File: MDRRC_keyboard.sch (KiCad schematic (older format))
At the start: 16 parts

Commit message: Fixed two small errors
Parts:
- gave numbers to parts that had none: 16
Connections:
- net GND: now also CON1.6
- net VCC: now also C4.1, P3.1 (P1), R4.1, R5.1
- net at IC1.8 (PB7(XTAL2/TOSC2)), P2.8 (P8): no longer CON1.6
- new net: D1.2 (K), IC1.14 ((~SS~/OC1B)PB2)
- no-connect marks 0 -> 12
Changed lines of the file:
@@
-EESchema Schematic File Version 2  date Sunday, 2013 September 29 10:10:44
+EESchema Schematic File Version 2  date Sunday, 2013 September 29 16:19:32
 LIBS:power
 LIBS:device
@@
 LIBS:valves
 LIBS:pyth
+LIBS:MDRRC_keyboard-cache
 EELAYER 27 0
 EELAYER END
@@
 $EndDescr
 $Comp
-L LCD P?
+L LCD P1
 U 1 1 52473158
 P 6750 3100
-F 0 "P?" V 6850 3100 60  0000 C CNN
+F 0 "P1" V 6850 3100 60  0000 C CNN
 F 1 "LCD" V 6950 3100 60  0000 C CNN
 F 2 "" H 6750 3100 60  0000 C CNN
@@
 	10650 2850 10750 2950
 $Comp
-L ATMEGA8-AI IC?
+L ATMEGA8-AI IC1
 U 1 1 52473167
 P 4350 3200
-F 0 "IC?" H 3650 4350 50  0000 L BNN
+F 0 "IC1" H 3650 4350 50  0000 L BNN
 F 1 "ATMEGA8-AI" H 4650 1700 50  0000 L BNN
 F 2 "TQFP32" H 3800 1750 50  0001 C CNN
@@
 $EndComp
 $Comp
-L CONN_8 P?
+L CONN_8 P2
 U 1 1 52473176
 P 6750 4350
-F 0 "P?" V 6700 4350 60  0000 C CNN
+F 0 "P2" V 6700 4350 60  0000 C CNN
 F 1 "CONN_8" V 6800 4350 60  0000 C CNN
 F 2 "" H 6750 4350 60  0000 C CNN
@@
 Wire Wire Line
 	6050 4600 6400 4600
-Wire Wire Line
-	3450 3100 3400 3100
-Wire Wire Line
-	3400 3100 3400 4700
-Wire Wire Line
-	3200 4700 6400 4700
-$Comp
-L GND #PWR?
+$Comp
+L GND #PWR01
 U 1 1 524731E3
 P 4350 4900
-F 0 "#PWR?" H 4350 4900 30  0001 C CNN
+F 0 "#PWR01" H 4350 4900 30  0001 C CNN
 F 1 "GND" H 4350 4830 30  0001 C CNN
 F 2 "" H 4350 4900 60  0000 C CNN
@@
 $EndComp
 $Comp
-L GND #PWR?
+L GND #PWR02
 U 1 1 524731F2
 P 6250 4900
-F 0 "#PWR?" H 6250 4900 30  0001 C CNN
+F 0 "#PWR02" H 6250 4900 30  0001 C CNN
 F 1 "GND" H 6250 4830 30  0001 C CNN
 F 2 "" H 6250 4900 60  0000 C CNN
@@
 	4300 4800 4300 4850
 Wire Wire Line
-	4300 4850 4400 4850
+	3200 4850 4400 4850
 Wire Wire Line
 	4350 4850 4350 4900
@@
 Connection ~ 4350 4850
 $Comp
-L VCC #PWR?
+L VCC #PWR03
 U 1 1 52473237
 P 4350 1800
-F 0 "#PWR?" H 4350 1900 30  0001 C CNN
+F 0 "#PWR03" H 4350 1900 30  0001 C CNN
 F 1 "VCC" H 4350 1900 30  0000 C CNN
 F 2 "" H 4350 1800 60  0000 C CNN
@@
 $EndComp
 $Comp
-L VCC #PWR?
+L VCC #PWR04
 U 1 1 52473246
 P 6350 1800
-F 0 "#PWR?" H 6350 1900 30  0001 C CNN
+F 0 "#PWR04" H 6350 1900 30  0001 C CNN
 F 1 "VCC" H 6350 1900 30  0000 C CNN
 F 2 "" H 6350 1800 60  0000 C CNN
@@
 Connection ~ 4350 1850
 $Comp
-L POT RV?
+L POT RV1
 U 1 1 524732F4
 P 6050 1900
-F 0 "RV?" H 6050 1800 50  0000 C CNN
+F 0 "RV1" H 6050 1800 50  0000 C CNN
 F 1 "10k" H 6050 1900 50  0000 C CNN
 F 2 "" H 6050 1900 60  0000 C CNN
@@
 $EndComp
 Wire Wire Line
-	6300 1900 6350 1900
+	6300 1900 7500 1900
 Connection ~ 6350 1900
 Wire Wire Line
@@
 	5800 3600 6400 3600
 $Comp
-L C C?
+L C C3
 U 1 1 5247DC1C
 P 3150 2850
-F 0 "C?" H 3200 2950 50  0000 L CNN
+F 0 "C3" H 3200 2950 50  0000 L CNN
 F 1 "100nF" H 3200 2750 50  0000 L CNN
 F 2 "" H 3150 2850 60  0000 C CNN
@@
 Wire Wire Line
 	3150 2350 3150 2650
-Wire Wire Line
-	2700 2400 3450 2400
 Connection ~ 3150 2500
 $Comp
-L VCC #PWR?
+L VCC #PWR05
 U 1 1 5247DCDF
 P 3150 2350
-F 0 "#PWR?" H 3150 2450 30  0001 C CNN
+F 0 "#PWR05" H 3150 2450 30  0001 C CNN
 F 1 "VCC" H 3150 2450 30  0000 C CNN
 F 2 "" H 3150 2350 60  0000 C CNN
@@
 $EndComp
 $Comp
-L GND #PWR?
+L GND #PWR06
 U 1 1 5247DCEE
 P 3050 3150
-F 0 "#PWR?" H 3050 3150 30  0001 C CNN
+F 0 "#PWR06" H 3050 3150 30  0001 C CNN
 F 1 "GND" H 3050 3080 30  0001 C CNN
 F 2 "" H 3050 3150 60  0000 C CNN
@@
 Connection ~ 3150 2400
 $Comp
-L C C?
+L C C2
 U 1 1 5247DE1A
 P 2700 2850
-F 0 "C?" H 2750 2950 50  0000 L CNN
+F 0 "C2" H 2750 2950 50  0000 L CNN
 F 1 "100nF" H 2750 2750 50  0000 L CNN
 F 2 "" H 2700 2850 60  0000 C CNN
@@
 $EndComp
 Wire Wire Line
-	2700 2650 2700 2400
-Wire Wire Line
 	2700 3050 2700 3100
 Connection ~ 2950 3100
 $Comp
-L C C?
+L C C1
 U 1 1 5247DEB3
 P 2400 2850
-F 0 "C?" H 2450 2950 50  0000 L CNN
+F 0 "C1" H 2450 2950 50  0000 L CNN
 F 1 "100nF" H 2450 2750 50  0000 L CNN
 F 2 "" H 2400 2850 60  0000 C CNN
@@
 $EndComp
 $Comp
-L R R?
+L R R1
 U 1 1 5247DEC2
 P 3350 1850
-F 0 "R?" V 3430 1850 50  0000 C CNN
+F 0 "R1" V 3430 1850 50  0000 C CNN
 F 1 "10k" V 3350 1850 50  0000 C CNN
 F 2 "" H 3350 1850 60  0000 C CNN
@@
 Connection ~ 3050 1850
 $Comp
-L R R?
+L R R3
 U 1 1 5247E01F
 P 7250 3500
-F 0 "R?" V 7330 3500 50  0000 C CNN
+F 0 "R3" V 7330 3500 50  0000 C CNN
 F 1 "1k" V 7250 3500 50  0000 C CNN
 F 2 "" H 7250 3500 60  0000 C CNN
@@
 $EndComp
 $Comp
-L LED D?
+L LED D1
 U 1 1 5247E02E
 P 7250 2950
-F 0 "D?" H 7250 3050 50  0000 C CNN
+F 0 "D1" H 7250 3050 50  0000 C CNN
 F 1 "LED" H 7250 2850 50  0000 C CNN
 F 2 "" H 7250 2950 60  0000 C CNN
@@
 	6000 2400 6000 2150
 Wire Wire Line
-	6000 2150 7850 2150
-Wire Wire Line
 	7250 2150 7250 2750
 Wire Wire Line
@@
 Connection ~ 6250 4800
 $Comp
-L CONN_4 P?
+L CONN_4 P3
 U 1 1 5247E156
 P 8250 3300
-F 0 "P?" V 8200 3300 50  0000 C CNN
+F 0 "P3" V 8200 3300 50  0000 C CNN
 F 1 "CONN_4" V 8300 3300 50  0000 C CNN
 F 2 "" H 8250 3300 60  0000 C CNN
@@
 Wire Wire Line
 	7850 2150 7850 3150
-Connection ~ 7250 2150
 Text Label 5500 3300 0    60   ~ 0
 SDA
@@
 	7500 3350 7900 3350
 $Comp
-L R R?
+L R R4
 U 1 1 5247E4A3
 P 7500 2700
-F 0 "R?" V 7580 2700 50  0000 C CNN
+F 0 "R4" V 7580 2700 50  0000 C CNN
 F 1 "10k" V 7500 2700 50  0000 C CNN
 F 2 "" H 7500 2700 60  0000 C CNN
@@
 $EndComp
 $Comp
-L R R?
+L R R5
 U 1 1 5247E4B2
 P 7700 2700
-F 0 "R?" V 7780 2700 50  0000 C CNN
+F 0 "R5" V 7780 2700 50  0000 C CNN
 F 1 "10k" V 7700 2700 50  0000 C CNN
 F 2 "" H 7700 2700 60  0000 C CNN
@@
 Connection ~ 7700 2150
 Wire Wire Line
-	7500 2450 7500 2150
+	7500 1900 7500 2450
 Connection ~ 7500 2150
 $Comp
-L C C?
+L C C4
 U 1 1 5247E729
 P 7800 3950
-F 0 "C?" H 7850 4050 50  0000 L CNN
+F 0 "C4" H 7850 4050 50  0000 L CNN
 F 1 "100nF" H 7850 3850 50  0000 L CNN
 F 2 "" H 7800 3950 60  0000 C CNN
@@
 Connection ~ 6250 3800
 $Comp
-L R R?
+L R R2
 U 1 1 5247E934
 P 5800 3700
-F 0 "R?" V 5880 3700 50  0000 C CNN
+F 0 "R2" V 5880 3700 50  0000 C CNN
 F 1 "4k7" V 5800 3700 50  0000 C CNN
 F 2 "" H 5800 3700 60  0000 C CNN
@@
 Connection ~ 4400 1850
 Wire Wire Line
-	3200 4250 3200 4700
-Connection ~ 3400 4700
-Wire Wire Line
-	3300 4050 3300 2400
+	3200 4250 3200 4850
+Wire Wire Line
+	3300 2400 3300 4050
 Connection ~ 3300 2400
 Wire Wire Line
@@
 Connection ~ 3050 2200
 $Comp
-L AVR-ISP-6 CON?
+L AVR-ISP-6 CON1
 U 1 1 5247F672
 P 2800 4150
-F 0 "CON?" H 2720 4390 50  0000 C CNN
+F 0 "CON1" H 2720 4390 50  0000 C CNN
 F 1 "AVR-ISP-6" H 2560 3920 50  0000 L BNN
 F 2 "AVR-ISP-6" V 2280 4190 50  0001 C CNN
@@
 $EndComp
 Wire Wire Line
-	2950 4050 3300 4050
+	3300 4050 2950 4050
 Wire Wire Line
 	2950 4250 3200 4250
@@
 	5700 2100 5700 2700
 Connection ~ 5700 2700
+NoConn ~ 5300 2250
+NoConn ~ 5350 2300
+NoConn ~ 5350 2900
+NoConn ~ 5350 3500
+NoConn ~ 5350 3600
+NoConn ~ 5350 3800
+NoConn ~ 5350 3900
+NoConn ~ 3450 2900
+NoConn ~ 6400 2900
+NoConn ~ 6400 3000
+NoConn ~ 6400 3200
+NoConn ~ 6400 3100
+Wire Wire Line
+	2700 2650 2700 2400
+Wire Wire Line
+	2700 2400 3450 2400
+Wire Wire Line
+	6000 2150 7250 2150
+Wire Wire Line
+	7500 2150 7850 2150
+Wire Wire Line
+	3450 3100 3400 3100
+Wire Wire Line
+	3400 3100 3400 4750
+Wire Wire Line
+	3400 4750 6200 4750
+Wire Wire Line
+	6200 4750 6200 4700
+Wire Wire Line
+	6200 4700 6400 4700
+Connection ~ 4300 4850
 $EndSCHEMATC

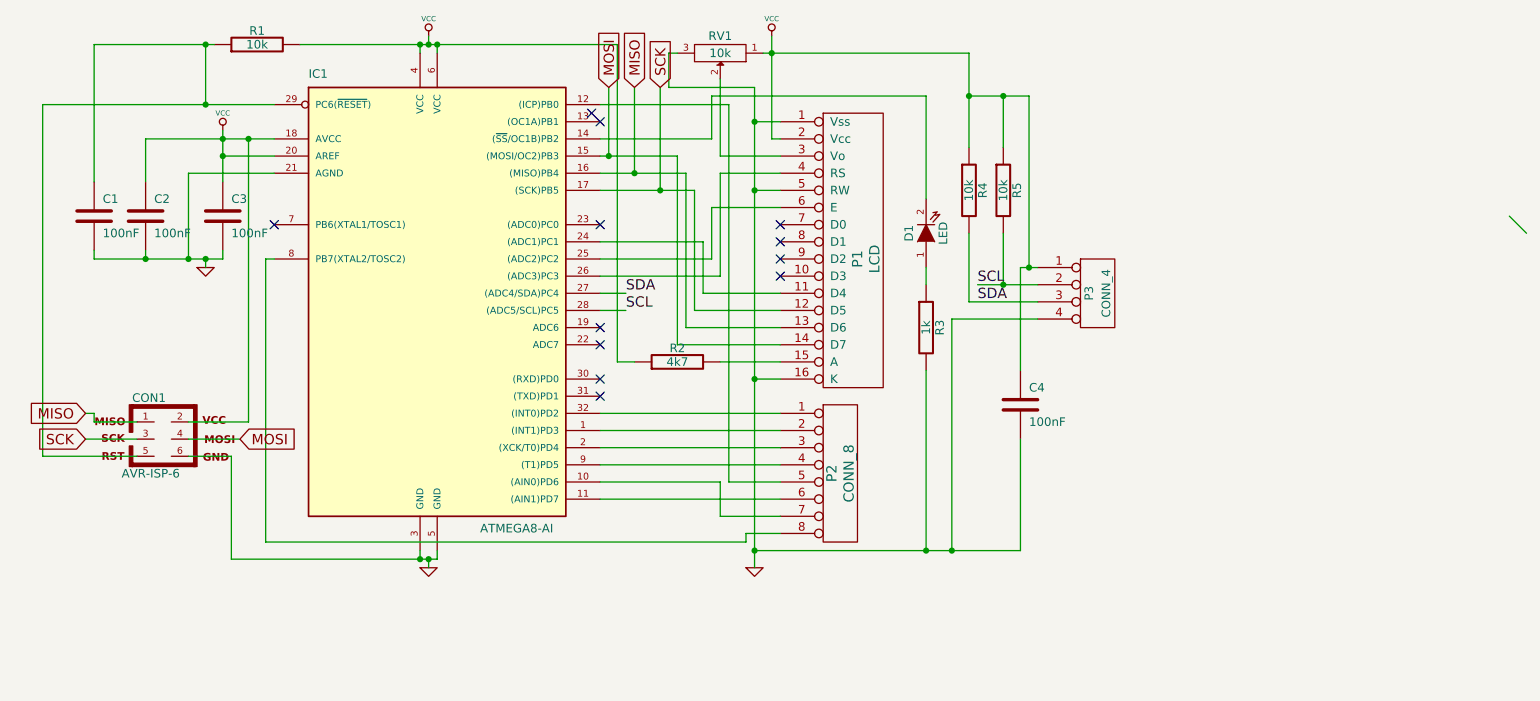
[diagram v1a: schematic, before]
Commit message: Added possibility for crystal and broke out remaining I/O to header
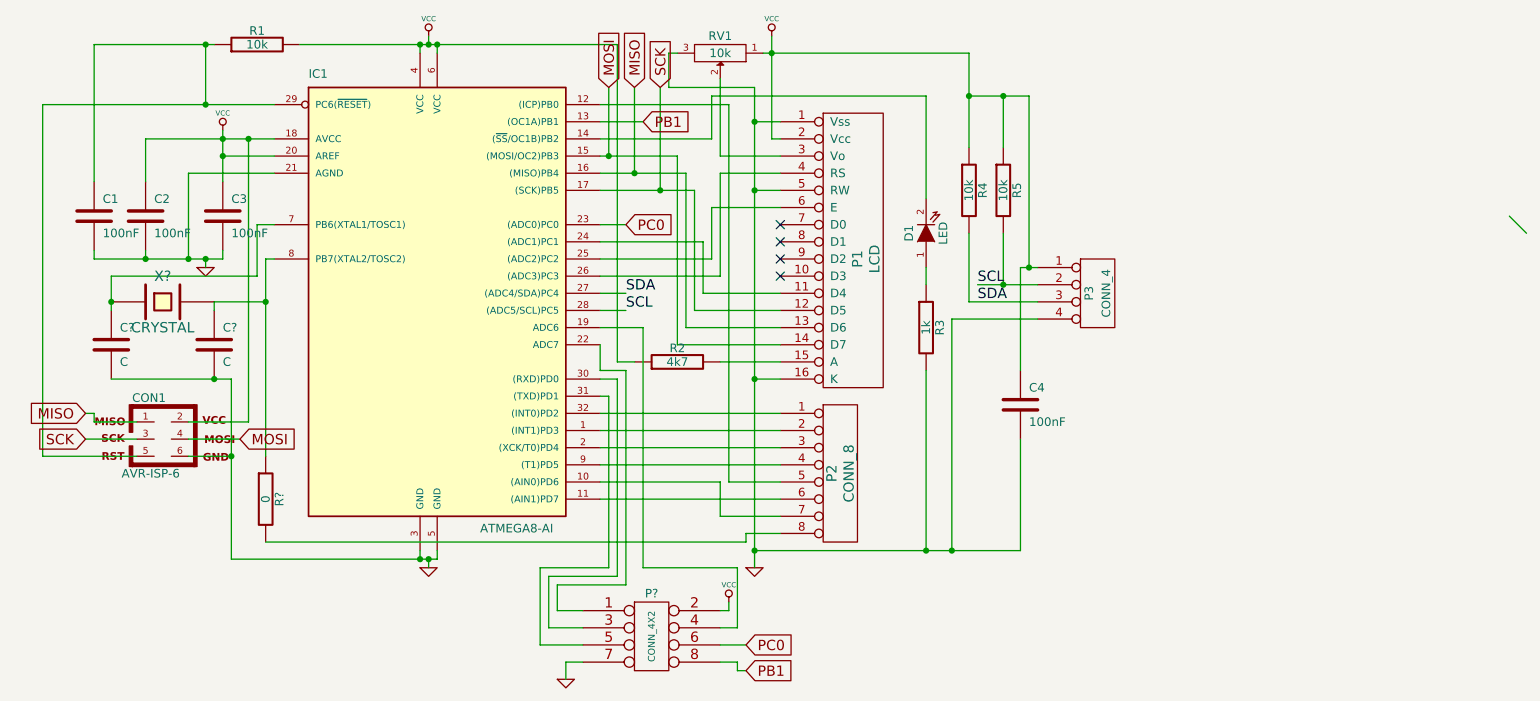
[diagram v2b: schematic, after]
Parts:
- added C? (x2): C, symbol C
- added P?: CONN_4X2, symbol CONN_4X2
- added R?: 0, symbol R
- added X?: CRYSTAL, symbol CRYSTAL
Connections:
- net GND: now also C?.2, C?.2, P?.7
- net VCC: now also P?.2
- net PB1: now reaches IC1.13 ((OC1A)PB1)
- net PB1: now also P?.8
- net at IC1.19 (ADC6): now also P?.4
- net at IC1.22 (ADC7): now also P?.1
- net PC0: now reaches IC1.23 ((ADC0)PC0)
- net PC0: now also P?.6
- net at IC1.30 ((RXD)PD0): now also P?.3
- net at IC1.31 ((TXD)PD1): now also P?.5
- net at IC1.7 (PB6(XTAL1/TOSC1)): now also C?.1, X?.1
- net at IC1.8 (PB7(XTAL2/TOSC2)): now also C?.1, R?.1, X?.2; no longer P2.8 (P8)
- new net: P2.8 (P8), R?.2
- no-connect marks 12 -> 4
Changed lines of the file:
@@
-EESchema Schematic File Version 2  date Sunday, 2013 September 29 16:19:32
+EESchema Schematic File Version 2  date Sunday, 2013 September 29 17:10:51
 LIBS:power
 LIBS:device
@@
 	10650 2850 10750 2950
 $Comp
-L ATMEGA8-AI IC1
-U 1 1 52473167
-P 4350 3200
-F 0 "IC1" H 3650 4350 50  0000 L BNN
-F 1 "ATMEGA8-AI" H 4650 1700 50  0000 L BNN
-F 2 "TQFP32" H 3800 1750 50  0001 C CNN
-F 3 "" H 4350 3200 60  0000 C CNN
-	1    4350 3200
-	1    0    0    -1
-$EndComp
-$Comp
 L CONN_8 P2
 U 1 1 52473176
@@
 Connection ~ 4400 1850
 Wire Wire Line
-	3200 4250 3200 4850
+	3200 3800 3200 4850
 Wire Wire Line
 	3300 2400 3300 4050
@@
 	5700 2100 5700 2700
 Connection ~ 5700 2700
-NoConn ~ 5300 2250
-NoConn ~ 5350 2300
-NoConn ~ 5350 2900
-NoConn ~ 5350 3500
-NoConn ~ 5350 3600
-NoConn ~ 5350 3800
-NoConn ~ 5350 3900
-NoConn ~ 3450 2900
 NoConn ~ 6400 2900
 NoConn ~ 6400 3000
@@
 	3450 3100 3400 3100
 Wire Wire Line
-	3400 3100 3400 4750
-Wire Wire Line
 	3400 4750 6200 4750
 Wire Wire Line
@@
 	6200 4700 6400 4700
 Connection ~ 4300 4850
+$Comp
+L R R?
+U 1 1 524841BC
+P 3400 4500
+F 0 "R?" V 3480 4500 50  0000 C CNN
+F 1 "0" V 3400 4500 50  0000 C CNN
+F 2 "" H 3400 4500 60  0000 C CNN
+F 3 "" H 3400 4500 60  0000 C CNN
+	1    3400 4500
+	1    0    0    -1
+$EndComp
+Wire Wire Line
+	3400 3100 3400 4250
+$Comp
+L C C?
+U 1 1 5248427B
+P 3100 3600
+F 0 "C?" H 3150 3700 50  0000 L CNN
+F 1 "C" H 3150 3500 50  0000 L CNN
+F 2 "" H 3100 3600 60  0000 C CNN
+F 3 "" H 3100 3600 60  0000 C CNN
+	1    3100 3600
+	1    0    0    -1
+$EndComp
+$Comp
+L C C?
+U 1 1 5248428A
+P 2500 3600
+F 0 "C?" H 2550 3700 50  0000 L CNN
+F 1 "C" H 2550 3500 50  0000 L CNN
+F 2 "" H 2500 3600 60  0000 C CNN
+F 3 "" H 2500 3600 60  0000 C CNN
+	1    2500 3600
+	1    0    0    -1
+$EndComp
+$Comp
+L CRYSTAL X?
+U 1 1 52484299
+P 2800 3350
+F 0 "X?" H 2800 3500 60  0000 C CNN
+F 1 "CRYSTAL" H 2800 3200 60  0000 C CNN
+F 2 "" H 2800 3350 60  0000 C CNN
+F 3 "" H 2800 3350 60  0000 C CNN
+	1    2800 3350
+	1    0    0    -1
+$EndComp
+Wire Wire Line
+	2500 3800 3200 3800
+Connection ~ 3200 4250
+Connection ~ 3100 3800
+Wire Wire Line
+	2500 3200 2500 3400
+Wire Wire Line
+	3100 3400 3100 3350
+Wire Wire Line
+	3100 3350 3400 3350
+Connection ~ 3400 3350
+Wire Wire Line
+	2500 3200 3350 3200
+Wire Wire Line
+	3350 3200 3350 2900
+Wire Wire Line
+	3350 2900 3450 2900
+Connection ~ 2500 3350
+$Comp
+L ATMEGA8-AI IC1
+U 1 1 52473167
+P 4350 3200
+F 0 "IC1" H 3650 4350 50  0000 L BNN
+F 1 "ATMEGA8-AI" H 4650 1700 50  0000 L BNN
+F 2 "TQFP32" H 3800 1750 50  0001 C CNN
+F 3 "" H 4350 3200 60  0000 C CNN
+	1    4350 3200
+	1    0    0    -1
+$EndComp
+$Comp
+L CONN_4X2 P?
+U 1 1 52484835
+P 5650 5300
+F 0 "P?" H 5650 5550 50  0000 C CNN
+F 1 "CONN_4X2" V 5650 5300 40  0000 C CNN
+F 2 "" H 5650 5300 60  0000 C CNN
+F 3 "" H 5650 5300 60  0000 C CNN
+	1    5650 5300
+	1    0    0    -1
+$EndComp
+$Comp
+L GND #PWR?
+U 1 1 52484844
+P 5150 5550
+F 0 "#PWR?" H 5150 5550 30  0001 C CNN
+F 1 "GND" H 5150 5480 30  0001 C CNN
+F 2 "" H 5150 5550 60  0000 C CNN
+F 3 "" H 5150 5550 60  0000 C CNN
+	1    5150 5550
+	1    0    0    -1
+$EndComp
+$Comp
+L VCC #PWR?
+U 1 1 52484853
+P 6100 5100
+F 0 "#PWR?" H 6100 5200 30  0001 C CNN
+F 1 "VCC" H 6100 5200 30  0000 C CNN
+F 2 "" H 6100 5100 60  0000 C CNN
+F 3 "" H 6100 5100 60  0000 C CNN
+	1    6100 5100
+	1    0    0    -1
+$EndComp
+Wire Wire Line
+	6100 5100 6100 5150
+Wire Wire Line
+	6100 5150 6050 5150
+Wire Wire Line
+	5250 5450 5150 5450
+Wire Wire Line
+	5150 5450 5150 5550
+Wire Wire Line
+	5350 3900 5400 3900
+Wire Wire Line
+	5400 3900 5400 4900
+Wire Wire Line
+	5400 4900 5000 4900
+Wire Wire Line
+	5000 4900 5000 5350
+Wire Wire Line
+	5000 5350 5250 5350
+Wire Wire Line
+	5350 3800 5450 3800
+Wire Wire Line
+	5450 3800 5450 4950
+Wire Wire Line
+	5450 4950 5050 4950
+Wire Wire Line
+	5050 4950 5050 5250
+Wire Wire Line
+	5050 5250 5250 5250
+Wire Wire Line
+	5350 3600 5350 3750
+Wire Wire Line
+	5350 3750 5500 3750
+Wire Wire Line
+	5500 3750 5500 5000
+Wire Wire Line
+	5500 5000 5100 5000
+Wire Wire Line
+	5100 5000 5100 5150
+Wire Wire Line
+	5100 5150 5250 5150
+Wire Wire Line
+	5350 3500 5600 3500
+Wire Wire Line
+	5600 3500 5600 4900
+Wire Wire Line
+	5600 4900 6150 4900
+Wire Wire Line
+	6150 4900 6150 5250
+Wire Wire Line
+	6150 5250 6050 5250
+Text GLabel 5500 2900 2    60   Input ~ 0
+PC0
+Text GLabel 5600 2300 2    60   Input ~ 0
+PB1
+Wire Wire Line
+	5600 2300 5350 2300
+Wire Wire Line
+	5500 2900 5350 2900
+Text GLabel 6200 5350 2    60   Input ~ 0
+PC0
+Text GLabel 6200 5500 2    60   Input ~ 0
+PB1
+Wire Wire Line
+	6200 5500 6150 5500
+Wire Wire Line
+	6150 5500 6150 5450
+Wire Wire Line
+	6150 5450 6050 5450
+Wire Wire Line
+	6200 5350 6050 5350
 $EndSCHEMATC

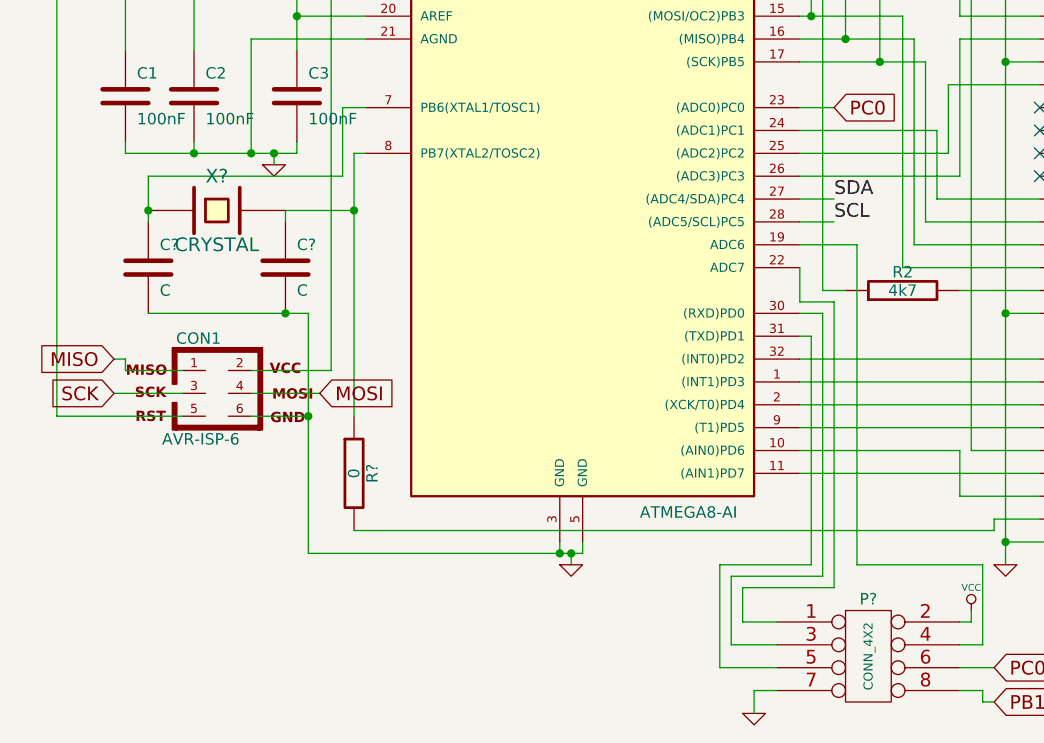
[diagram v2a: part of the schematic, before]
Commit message: Updated board to include previous changes to schematic
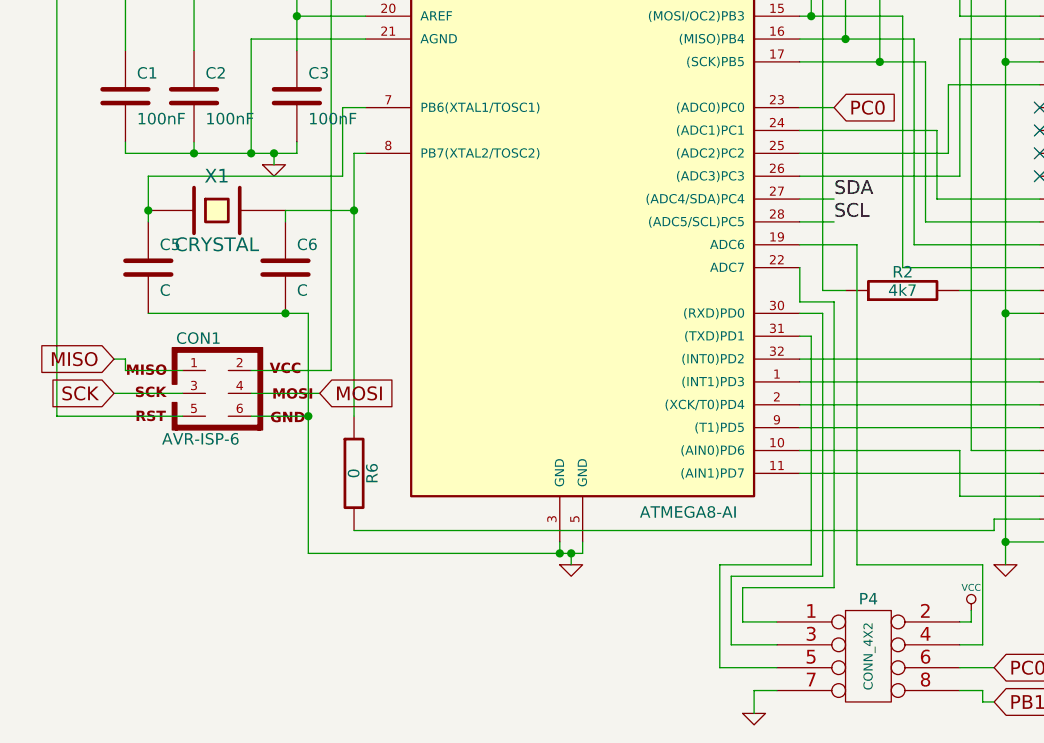
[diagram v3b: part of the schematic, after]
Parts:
- gave numbers to parts that had none: 5
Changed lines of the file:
@@
-EESchema Schematic File Version 2  date Sunday, 2013 September 29 17:10:51
+EESchema Schematic File Version 2  date Sunday, 2013 September 29 17:15:11
 LIBS:power
 LIBS:device
@@
 Connection ~ 4300 4850
 $Comp
-L R R?
+L R R6
 U 1 1 524841BC
 P 3400 4500
-F 0 "R?" V 3480 4500 50  0000 C CNN
+F 0 "R6" V 3480 4500 50  0000 C CNN
 F 1 "0" V 3400 4500 50  0000 C CNN
 F 2 "" H 3400 4500 60  0000 C CNN
@@
 	3400 3100 3400 4250
 $Comp
-L C C?
+L C C6
 U 1 1 5248427B
 P 3100 3600
-F 0 "C?" H 3150 3700 50  0000 L CNN
+F 0 "C6" H 3150 3700 50  0000 L CNN
 F 1 "C" H 3150 3500 50  0000 L CNN
 F 2 "" H 3100 3600 60  0000 C CNN
@@
 $EndComp
 $Comp
-L C C?
+L C C5
 U 1 1 5248428A
 P 2500 3600
-F 0 "C?" H 2550 3700 50  0000 L CNN
+F 0 "C5" H 2550 3700 50  0000 L CNN
 F 1 "C" H 2550 3500 50  0000 L CNN
 F 2 "" H 2500 3600 60  0000 C CNN
@@
 $EndComp
 $Comp
-L CRYSTAL X?
+L CRYSTAL X1
 U 1 1 52484299
 P 2800 3350
-F 0 "X?" H 2800 3500 60  0000 C CNN
+F 0 "X1" H 2800 3500 60  0000 C CNN
 F 1 "CRYSTAL" H 2800 3200 60  0000 C CNN
 F 2 "" H 2800 3350 60  0000 C CNN
@@
 $EndComp
 $Comp
-L CONN_4X2 P?
+L CONN_4X2 P4
 U 1 1 52484835
 P 5650 5300
-F 0 "P?" H 5650 5550 50  0000 C CNN
+F 0 "P4" H 5650 5550 50  0000 C CNN
 F 1 "CONN_4X2" V 5650 5300 40  0000 C CNN
 F 2 "" H 5650 5300 60  0000 C CNN
@@
 $EndComp
 $Comp
-L GND #PWR?
+L GND #PWR07
 U 1 1 52484844
 P 5150 5550
-F 0 "#PWR?" H 5150 5550 30  0001 C CNN
+F 0 "#PWR07" H 5150 5550 30  0001 C CNN
 F 1 "GND" H 5150 5480 30  0001 C CNN
 F 2 "" H 5150 5550 60  0000 C CNN
@@
 $EndComp
 $Comp
-L VCC #PWR?
+L VCC #PWR08
 U 1 1 52484853
 P 6100 5100
-F 0 "#PWR?" H 6100 5200 30  0001 C CNN
+F 0 "#PWR08" H 6100 5200 30  0001 C CNN
 F 1 "VCC" H 6100 5200 30  0000 C CNN
 F 2 "" H 6100 5100 60  0000 C CNN
